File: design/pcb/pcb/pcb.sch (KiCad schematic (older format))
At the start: 11 parts, among them J1 Conn_01x10_Male, J10 shock_grid, J11 shock_grid, J2 Conn_01x10_Male, J3 Conn_02x10_Top_Bottom, J4 shock_grid, J5 shock_grid, J6 shock_grid, J7 shock_grid, J8 shock_grid, J9 shock_grid

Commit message: Made two custom (S/D)IP footprints with slightly larger clearances. Mostly fixed custom electrode footprint pad anchor points.
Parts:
- J1, J2: footprint Connectors_Molex:Molex_KK-6410-10_10x2.54mm_Straight -> footprints:SIP-10_2.54mm_1mm_clearance
- J3: footprint Connectors_Multicomp:Multicomp_MC9A12-2034_2x10x2.54mm_Straight -> footprints:DIP-2x10_2.54mm_1mm_clearance
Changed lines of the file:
@@
 F 0 "J3" H 1200 2417 50  0000 C CNN
 F 1 "Conn_02x10_Top_Bottom" H 1200 2326 50  0000 C CNN
-F 2 "Connectors_Multicomp:Multicomp_MC9A12-2034_2x10x2.54mm_Straight" H 1150 1800 50  0001 C CNN
+F 2 "footprints:DIP-2x10_2.54mm_1mm_clearance" H 1150 1800 50  0001 C CNN
 F 3 "" H 1150 1800 50  0001 C CNN
 	1    1150 1800
@@
 F 0 "J2" H 1206 5078 50  0000 C CNN
 F 1 "Conn_01x10_Male" H 1206 4987 50  0000 C CNN
-F 2 "Connectors_Molex:Molex_KK-6410-10_10x2.54mm_Straight" H 1100 4500 50  0001 C CNN
+F 2 "footprints:SIP-10_2.54mm_1mm_clearance" H 1100 4500 50  0001 C CNN
 F 3 "" H 1100 4500 50  0001 C CNN
 	1    1100 4500
@@
 F 0 "J1" H 1206 3928 50  0000 C CNN
 F 1 "Conn_01x10_Male" H 1206 3837 50  0000 C CNN
-F 2 "Connectors_Molex:Molex_KK-6410-10_10x2.54mm_Straight" H 1100 3350 50  0001 C CNN
+F 2 "footprints:SIP-10_2.54mm_1mm_clearance" H 1100 3350 50  0001 C CNN
 F 3 "" H 1100 3350 50  0001 C CNN
 	1    1100 3350

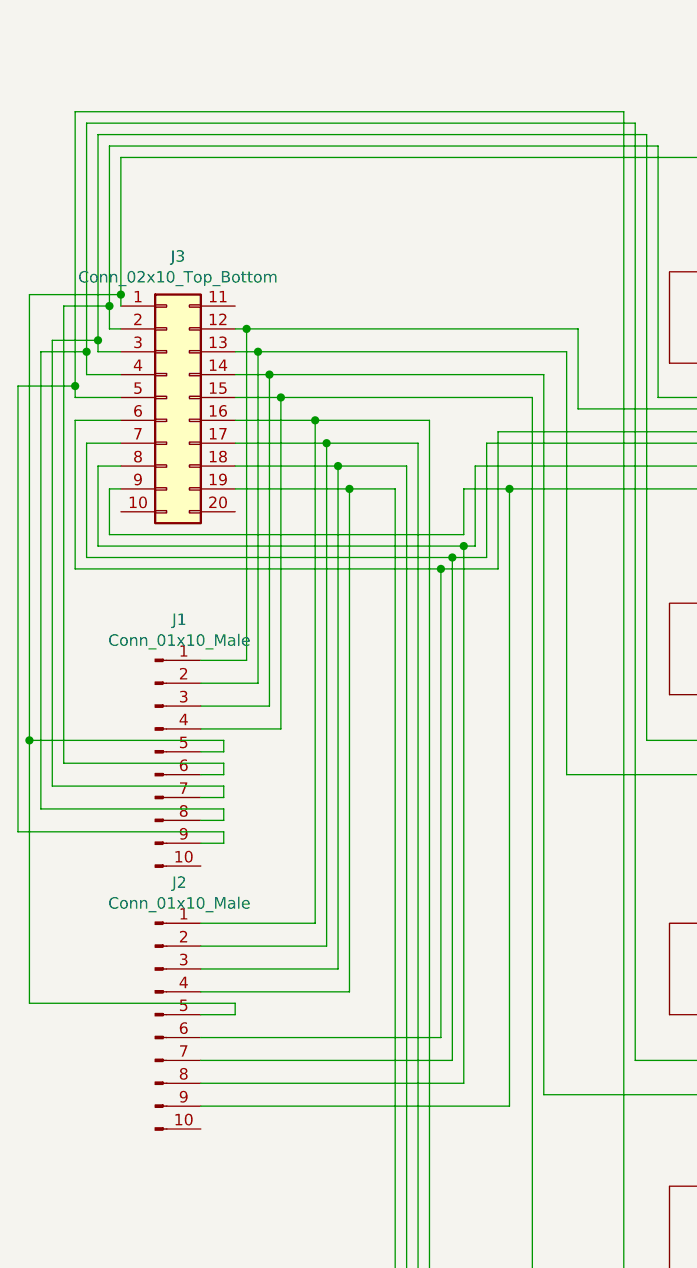
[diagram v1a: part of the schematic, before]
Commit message: Re-ordered some pins in sch and regenerated netlist. Increased y margin to connectors for extra space for routing. Finished routing of board with original footprint geometry.
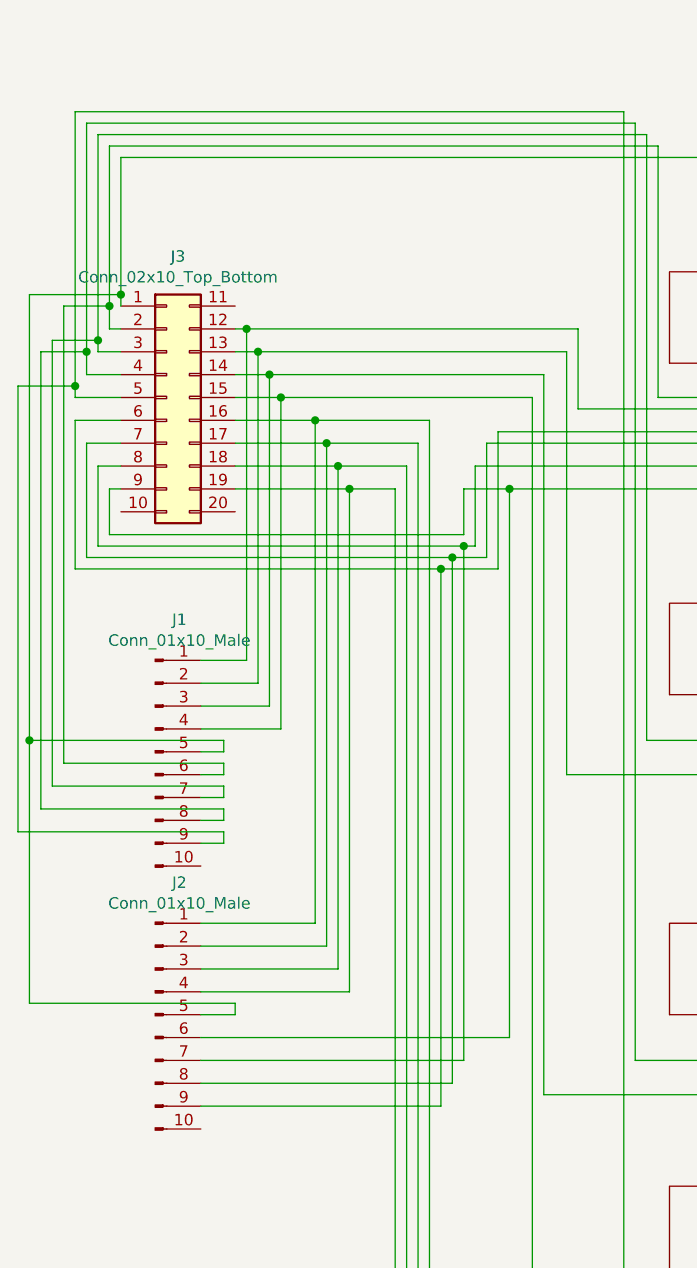
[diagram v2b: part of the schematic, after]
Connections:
- net at J3.6 (Pin_6), J8.1 (left_grid): now also J2.9 (Pin_9); no longer J2.6 (Pin_6)
- net at J3.7 (Pin_7), J9.1 (left_grid): now also J2.8 (Pin_8); no longer J2.7 (Pin_7)
- net at J10.1 (left_grid), J3.8 (Pin_8): now also J2.7 (Pin_7); no longer J2.8 (Pin_8)
- net at J11.1 (left_grid), J3.9 (Pin_9): now also J2.6 (Pin_6); no longer J2.9 (Pin_9)
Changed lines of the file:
@@
 $EndComp
 Wire Wire Line
-	950  1400 950  750
+	950  750  950  1400
 Wire Wire Line
 	950  750  5850 750
@@
 Connection ~ 5850 5100
 Wire Wire Line
-	950  1500 900  1500
-Wire Wire Line
-	900  1500 900  700
+	900  1500 950  1500
+Wire Wire Line
+	900  700  900  1500
 Wire Wire Line
 	900  700  3300 700
@@
 	3850 1800 3850 1650
 Wire Wire Line
-	950  1600 850  1600
-Wire Wire Line
-	850  1600 850  650
+	850  1600 950  1600
+Wire Wire Line
+	850  650  850  1600
 Wire Wire Line
 	850  650  3250 650
@@
 	3850 3300 3850 3100
 Wire Wire Line
-	950  1700 800  1700
-Wire Wire Line
-	800  1700 800  600
+	800  1700 950  1700
+Wire Wire Line
+	800  600  800  1700
 Wire Wire Line
 	800  600  3200 600
@@
 	3850 4700 3850 4500
 Wire Wire Line
-	950  1800 750  1800
-Wire Wire Line
-	750  1800 750  550
+	750  1800 950  1800
+Wire Wire Line
+	750  550  750  1800
 Wire Wire Line
 	750  550  3150 550
@@
 Wire Wire Line
 	750  1900 750  2550
-Wire Wire Line
-	750  2550 2600 2550
 Wire Wire Line
 	2600 2550 2600 1950
@@
 Connection ~ 1600 1700
 Connection ~ 1650 1800
-Wire Wire Line
-	2350 2550 2350 4600
 Connection ~ 2350 2550
-Wire Wire Line
-	2400 2500 2400 4700
 Connection ~ 2400 2500
-Wire Wire Line
-	2450 2450 2450 4800
 Connection ~ 2450 2450
-Wire Wire Line
-	2650 2200 2650 4900
 Connection ~ 2650 2200
 Connection ~ 1800 1900
@@
 	1950 4400 1950 2200
 Wire Wire Line
-	2350 4600 1300 4600
-Wire Wire Line
-	2400 4700 1300 4700
-Wire Wire Line
-	2450 4800 1300 4800
-Wire Wire Line
-	2650 4900 1300 4900
+	750  2550 2600 2550
+Wire Wire Line
+	1300 4600 2650 4600
+Wire Wire Line
+	2650 4600 2650 2200
+Wire Wire Line
+	1300 4700 2450 4700
+Wire Wire Line
+	2450 4700 2450 2450
+Wire Wire Line
+	1300 4800 2400 4800
+Wire Wire Line
+	2400 4800 2400 2500
+Wire Wire Line
+	1300 4900 2350 4900
+Wire Wire Line
+	2350 4900 2350 2550
 $EndSCHEMATC
